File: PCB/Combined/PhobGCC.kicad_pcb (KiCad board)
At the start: 2 copper layers, 143 x 91.4 mm, 76 parts, among them J1 Conn_01x06_Female, J2 Conn_01x04_Female, J3 Conn_01x01_Male, J4 Conn_01x04_Male, J5 Rumble, Q1 Q_NMOS_GSD, Q2 Q_PMOS_GDS, Q3 Q_NMOS_GSD, SW1 A, SW10 Dup, SW11 Dright, SW12 Ddown, SW2 B, SW3 X, SW4 Y, SW5 Start, SW6 L, SW7 R, SW8 Z, SW9 Dleft, U1 Teensy4.0, U2 2x DRV5053CAQLPGM Hall Effect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, U3 GP2S60-MFG, U4 GP2S60-MFG, U5 Stickbox_Assembly

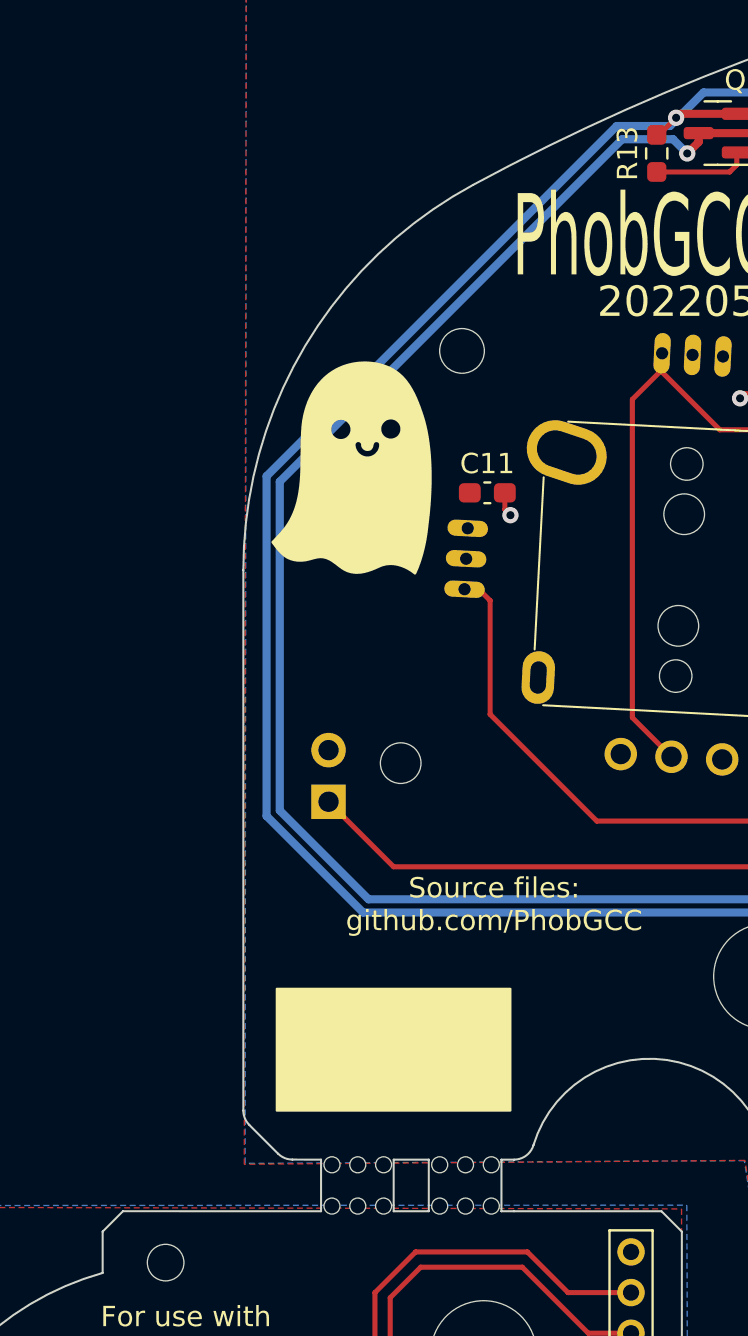
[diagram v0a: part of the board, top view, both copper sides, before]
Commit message: wide mousebites
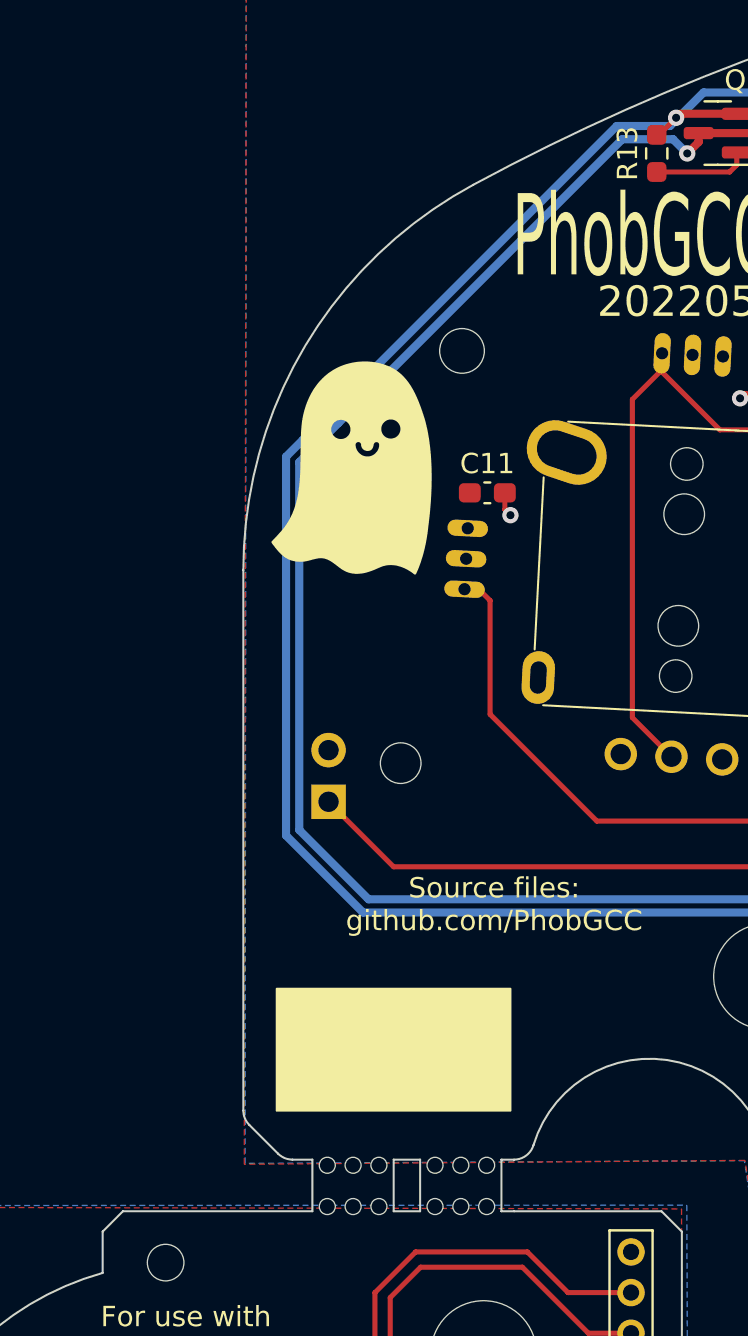
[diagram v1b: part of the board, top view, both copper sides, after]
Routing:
- net Net-(D2-Pad2): track 85.0 -> 84.2 mm
- net +5V: track 132.4 -> 131.6 mm
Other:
- outline, holes or cut-outs redrawn
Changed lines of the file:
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@@
       (effects (font (size 1 1) (thickness 0.15)))
     )
-    (fp_line (start 1.59 -2.53885) (end -1.6 -2.53885) (layer "Dwgs.User") (width 0.1))
-    (fp_line (start -1.59 0) (end 1.6 0) (layer "Dwgs.User") (width 0.1))
-    (fp_line (start -1.806 -2.538) (end -1.806 0.002) (layer "Edge.Cuts") (width 0.1))
+    (fp_line (start 1.59 -2.53885) (end -2.05 -2.53885) (layer "Dwgs.User") (width 0.1))
+    (fp_line (start -2.09 0) (end 1.6 0) (layer "Dwgs.User") (width 0.1))
     (fp_line (start 1.767 -2.537893) (end 1.767 0.002107) (layer "Edge.Cuts") (width 0.1))
-    (pad "" np_thru_hole circle (at 0 -0.254) (size 0.7874 0.7874) (drill 0.7874) (layers *.Cu *.Mask))
-    (pad "" np_thru_hole circle (at 0 -2.28485 180) (size 0.7874 0.7874) (drill 0.7874) (layers *.Cu *.Mask))
-    (pad "" np_thru_hole circle (at -1.27 -0.254) (size 0.7874 0.7874) (drill 0.7874) (layers *.Cu *.Mask))
-    (pad "" np_thru_hole circle (at 1.27 -2.28485 180) (size 0.7874 0.7874) (drill 0.7874) (layers *.Cu *.Mask))
-    (pad "" np_thru_hole circle (at -1.27 -2.28485 180) (size 0.7874 0.7874) (drill 0.7874) (layers *.Cu *.Mask))
-    (pad "" np_thru_hole circle (at 1.27 -0.254) (size 0.7874 0.7874) (drill 0.7874) (layers *.Cu *.Mask))
+    (fp_line (start -2.233 -2.537893) (end -2.233 0.002107) (layer "Edge.Cuts") (width 0.1))
+    (pad "" np_thru_hole circle (at 1.04 -2.26085 180) (size 0.7874 0.7874) (drill 0.7874) (layers *.Cu *.Mask))
+    (pad "" np_thru_hole circle (at -1.5 -2.26085 180) (size 0.7874 0.7874) (drill 0.7874) (layers *.Cu *.Mask))
+    (pad "" np_thru_hole circle (at -1.5 -0.23) (size 0.7874 0.7874) (drill 0.7874) (layers *.Cu *.Mask))
+    (pad "" np_thru_hole circle (at -0.23 -2.26085 180) (size 0.7874 0.7874) (drill 0.7874) (layers *.Cu *.Mask))
+    (pad "" np_thru_hole circle (at -0.23 -0.23) (size 0.7874 0.7874) (drill 0.7874) (layers *.Cu *.Mask))
+    (pad "" np_thru_hole circle (at 1.04 -0.23) (size 0.7874 0.7874) (drill 0.7874) (layers *.Cu *.Mask))
   )
   (footprint "Capacitor_SMD:C_0603_1608Metric_Pad1.08x0.95mm_HandSolder" (layer "F.Cu")
@@
       (effects (font (size 1 1) (thickness 0.15)))
     )
-    (fp_line (start 1.59 -2.53885) (end -1.6 -2.53885) (layer "Dwgs.User") (width 0.1))
-    (fp_line (start -1.59 0) (end 1.6 0) (layer "Dwgs.User") (width 0.1))
+    (fp_line (start 1.59 -2.53885) (end -2.05 -2.53885) (layer "Dwgs.User") (width 0.1))
+    (fp_line (start -2.09 0) (end 1.6 0) (layer "Dwgs.User") (width 0.1))
     (fp_line (start 1.767 -2.537893) (end 1.767 0.002107) (layer "Edge.Cuts") (width 0.1))
-    (fp_line (start -1.806 -2.538) (end -1.806 0.002) (layer "Edge.Cuts") (width 0.1))
-    (pad "" np_thru_hole circle (at -1.27 -2.28485 180) (size 0.7874 0.7874) (drill 0.7874) (layers *.Cu *.Mask))
-    (pad "" np_thru_hole circle (at 0 -2.28485 180) (size 0.7874 0.7874) (drill 0.7874) (layers *.Cu *.Mask))
-    (pad "" np_thru_hole circle (at -1.27 -0.254) (size 0.7874 0.7874) (drill 0.7874) (layers *.Cu *.Mask))
-    (pad "" np_thru_hole circle (at 1.27 -2.28485 180) (size 0.7874 0.7874) (drill 0.7874) (layers *.Cu *.Mask))
-    (pad "" np_thru_hole circle (at 0 -0.254) (size 0.7874 0.7874) (drill 0.7874) (layers *.Cu *.Mask))
-    (pad "" np_thru_hole circle (at 1.27 -0.254) (size 0.7874 0.7874) (drill 0.7874) (layers *.Cu *.Mask))
+    (fp_line (start -2.233 -2.537893) (end -2.233 0.002107) (layer "Edge.Cuts") (width 0.1))
+    (pad "" np_thru_hole circle (at -0.23 -2.26085 180) (size 0.7874 0.7874) (drill 0.7874) (layers *.Cu *.Mask))
+    (pad "" np_thru_hole circle (at 1.04 -0.23) (size 0.7874 0.7874) (drill 0.7874) (layers *.Cu *.Mask))
+    (pad "" np_thru_hole circle (at -0.23 -0.23) (size 0.7874 0.7874) (drill 0.7874) (layers *.Cu *.Mask))
+    (pad "" np_thru_hole circle (at 1.04 -2.26085 180) (size 0.7874 0.7874) (drill 0.7874) (layers *.Cu *.Mask))
+    (pad "" np_thru_hole circle (at -1.5 -0.23) (size 0.7874 0.7874) (drill 0.7874) (layers *.Cu *.Mask))
+    (pad "" np_thru_hole circle (at -1.5 -2.26085 180) (size 0.7874 0.7874) (drill 0.7874) (layers *.Cu *.Mask))
   )
   (footprint "PhobGCC_Footprints:MountingHole_2.0mm" (layer "F.Cu")
@@
   (gr_line (start 161.660995 107.607107) (end 173.942892 107.607107) (layer "Edge.Cuts") (width 0.1))
   (gr_line (start 166.697895 62.732132) (end 167.096672 62.038607) (layer "Edge.Cuts") (width 0.1))
-  (gr_arc (start 52.271319 107.407107) (mid 51.888636 107.330986) (end 51.564213 107.114213) (layer "Edge.Cuts") (width 0.1))
-  (gr_line (start 53.682 107.40985) (end 52.271319 107.407107) (layer "Edge.Cuts") (width 0.1))
+  (gr_arc (start 52.271319 107.41) (mid 51.888618 107.331786) (end 51.564213 107.114213) (layer "Edge.Cuts") (width 0.1))
+  (gr_line (start 53.255 107.409957) (end 52.271319 107.41) (layer "Edge.Cuts") (width 0.1))
   (gr_line (start 152.207106 98.407107) (end 152.207106 101.192893) (layer "Edge.Cuts") (width 0.1))
   (gr_line (start 153.621319 102.607107) (end 155.744915 102.607107) (layer "Edge.Cuts") (width 0.1))
@@
   (gr_line (start 132.399999 91.7) (end 132.814212 92.114213) (layer "Edge.Cuts") (width 0.1))
   (gr_line (start 49.857106 78.407107) (end 49.857106 104.992893) (layer "Edge.Cuts") (width 0.1))
-  (gr_line (start 57.255 109.949957) (end 58.983 109.949957) (layer "Edge.Cuts") (width 0.1))
+  (gr_line (start 57.255 109.949957) (end 58.556 109.949957) (layer "Edge.Cuts") (width 0.1))
   (gr_line (start 42.934 110.951) (end 42.934 112.985328) (layer "Edge.Cuts") (width 0.1))
   (gr_line (start 63.178 109.95) (end 62.556 109.949957) (layer "Edge.Cuts") (width 0.1))
-  (gr_line (start 53.682 109.94985) (end 43.934 109.947107) (layer "Edge.Cuts") (width 0.1))
+  (gr_line (start 53.255 109.949957) (end 43.934 109.947107) (layer "Edge.Cuts") (width 0.1))
   (gr_arc (start 122.314213 50.743856) (mid 122.530986 51.068279) (end 122.607106 51.450963) (layer "Edge.Cuts") (width 0.1))
   (gr_line (start 152.499999 101.9) (end 152.914212 102.314213) (layer "Edge.Cuts") (width 0.1))
-  (gr_line (start 57.255 107.409957) (end 58.983 107.409957) (layer "Edge.Cuts") (width 0.1))
+  (gr_line (start 57.255 107.409957) (end 58.556 107.409957) (layer "Edge.Cuts") (width 0.1))
   (gr_arc (start 168.607106 62.907107) (mid 173.575565 68.860378) (end 175.357106 76.407107) (layer "Edge.Cuts") (width 0.1))
   (gr_arc (start 61.181382 124.001563) (mid 60.931149 122.753612) (end 62.1791 122.503378) (layer "Edge.Cuts") (width 0.1))
@@
   (segment (start 82.5 54.9) (end 72.5 54.9) (width 0.4) (layer "B.Cu") (net 23))
   (segment (start 72.5 54.9) (end 70.84952 56.55048) (width 0.4) (layer "B.Cu") (net 23))
-  (segment (start 51.000001 73.781439) (end 51.000001 90.500001) (width 0.4) (layer "B.Cu") (net 23))
   (segment (start 80.2 97.5) (end 81.775 97.5) (width 0.4) (layer "B.Cu") (net 23))
+  (segment (start 52.77922 72.00222) (end 68.230961 56.55048) (width 0.4) (layer "B.Cu") (net 23))
   (segment (start 81.775 97.5) (end 83.375 95.9) (width 0.4) (layer "B.Cu") (net 23))
-  (segment (start 51.000001 90.500001) (end 55.749519 95.249519) (width 0.4) (layer "B.Cu") (net 23))
   (segment (start 103.6 51.6) (end 103 51) (width 0.4) (layer "B.Cu") (net 23))
+  (segment (start 51.95848 91.45848) (end 51.95848 72.82296) (width 0.4) (layer "B.Cu") (net 23))
   (segment (start 77.94952 95.24952) (end 80.2 97.5) (width 0.4) (layer "B.Cu") (net 23))
   (segment (start 103 51) (end 93.5 51) (width 0.4) (layer "B.Cu") (net 23))
   (segment (start 70.84952 56.55048) (end 68.230961 56.55048) (width 0.4) (layer "B.Cu") (net 23))
-  (segment (start 68.230961 56.55048) (end 51.000001 73.781439) (width 0.4) (layer "B.Cu") (net 23))
+  (segment (start 51.95848 72.82296) (end 52.77922 72.00222) (width 0.4) (layer "B.Cu") (net 23))
   (segment (start 55.749519 95.249519) (end 77.94952 95.24952) (width 0.4) (layer "B.Cu") (net 23))
+  (segment (start 55.749519 95.249519) (end 51.95848 91.45848) (width 0.4) (layer "B.Cu") (net 23))
   (segment (start 103.6 52.9) (end 103.6 51.6) (width 0.4) (layer "B.Cu") (net 23))
   (segment (start 84.2 56.6) (end 82.5 54.9) (width 0.4) (layer "B.Cu") (net 23))
@@
   (segment (start 72.2625 56.9) (end 72.2625 57.3375) (width 0.4) (layer "F.Cu") (net 39))
   (via (at 71.7 57.9) (size 0.8) (drill 0.4) (layers "F.Cu" "B.Cu") (net 39))
-  (segment (start 68.5 57.2) (end 51.64952 74.05048) (width 0.4) (layer "B.Cu") (net 39))
   (segment (start 71 57.2) (end 68.5 57.2) (width 0.4) (layer "B.Cu") (net 39))
-  (segment (start 51.64952 74.05048) (end 51.64952 90.23096) (width 0.4) (layer "B.Cu") (net 39))
+  (segment (start 56.01856 94.6) (end 52.608 91.18944) (width 0.4) (layer "B.Cu") (net 39))
   (segment (start 79.51856 95.9) (end 80.835 95.9) (width 0.4) (layer "B.Cu") (net 39))
+  (segment (start 52.608 91.18944) (end 52.608 73.092) (width 0.4) (layer "B.Cu") (net 39))
   (segment (start 71.7 57.9) (end 71 57.2) (width 0.4) (layer "B.Cu") (net 39))
   (segment (start 78.21856 94.6) (end 79.51856 95.9) (width 0.4) (layer "B.Cu") (net 39))
-  (segment (start 51.64952 90.23096) (end 56.01856 94.6) (width 0.4) (layer "B.Cu") (net 39))
+  (segment (start 52.608 73.092) (end 54.544 71.156) (width 0.4) (layer "B.Cu") (net 39))
+  (segment (start 68.5 57.2) (end 54.544 71.156) (width 0.4) (layer "B.Cu") (net 39))
   (segment (start 56.01856 94.6) (end 78.21856 94.6) (width 0.4) (layer "B.Cu") (net 39))
   (segment (start 107.2 54.55) (end 108.8 56.15) (width 0.25) (layer "F.Cu") (net 40))

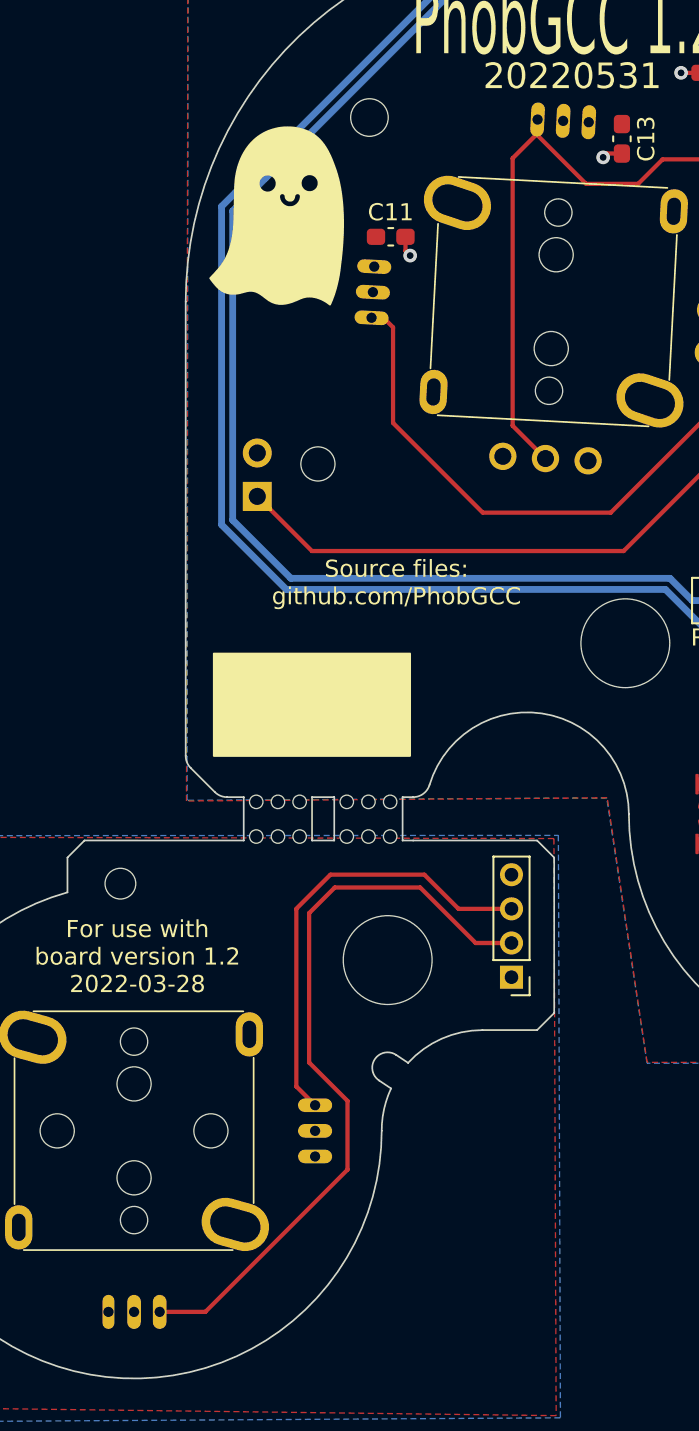
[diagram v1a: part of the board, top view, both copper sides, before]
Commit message: fixed footprints
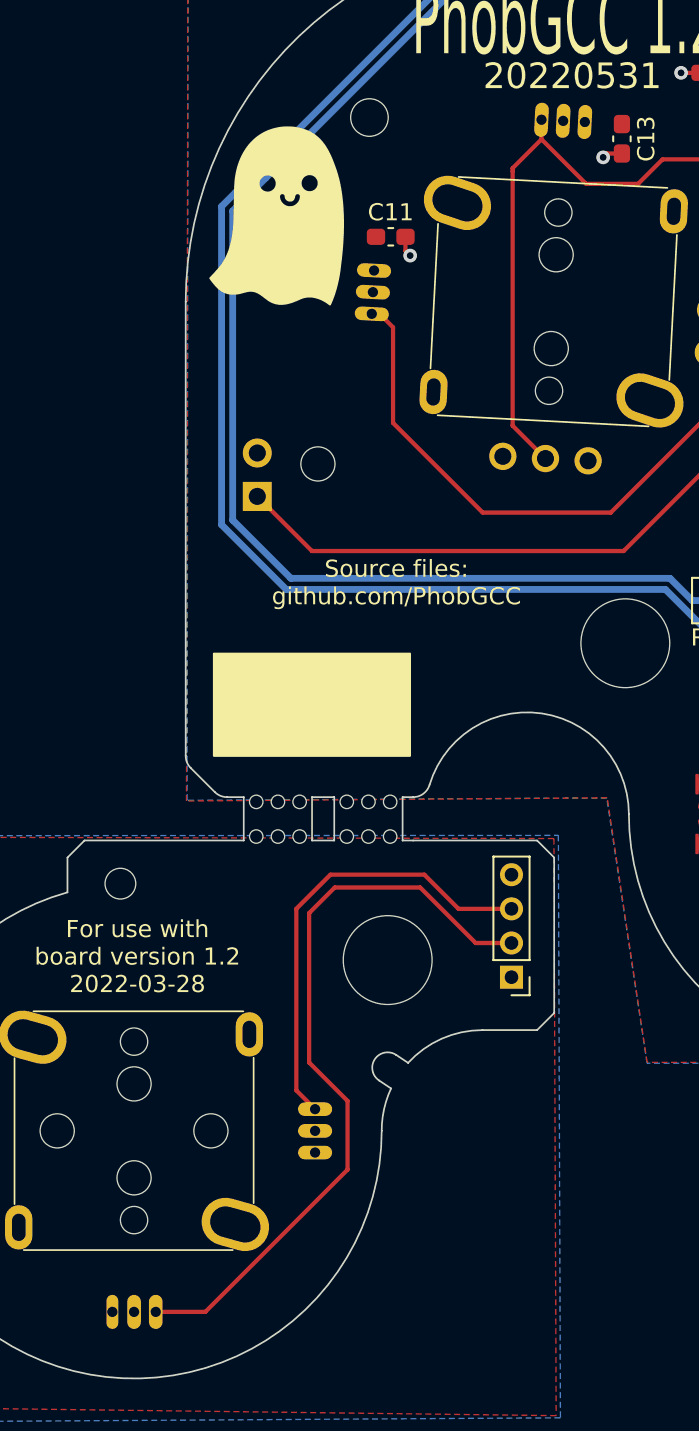
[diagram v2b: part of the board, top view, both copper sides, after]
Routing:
- net /Stick_y: track 47.1 -> 47.9 mm
